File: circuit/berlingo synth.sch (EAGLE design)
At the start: 56 parts, among them IC4 LM358N

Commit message: Changed order and added stereo
Changed order to IN - VCO - VCO~ - LFO - LED - PWM in - PWM~ - PWM out -
FILTER in - FILTER OUT - OUT - OUT

Added L and R
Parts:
- removed C1: 100uF, resistor:C-US050-075X075
- removed JP1: BAT_VIN, adafruit:PINHD-1X1CB
- removed LFO_PHOTO, TRI_PHOTO: PHOTOCELLPTH, SparkFun-Sensors:PHOTOCELLPTH
- removed OUT_C1: 22uF (226), SparkFun-Capacitors:CAPEZ
- removed OUT_R1, OUT_R2: 150, resistor:R-US_0207/10
- added BAT_V+: (no value), wirepad:3,81/1,4
- added C2: 100uF, rcl:CPOL-USE2-4
- added C_OUT_L, C_OUT_R, IN_C2: 226, SparkFun-Capacitors:CAPEZ
- added H6: MOUNT-HOLE2.8, holes:MOUNT-HOLE2.8
- added IN_R: IN(R), TOF:HEADER-1X1
- added IN_R3, IN_R4: 10k, resistor:R-US_0207/10
- added SW1: OS102011MA1Q, adafruit:OS102011MA1Q
- BAT_GND: device adafruit:PINHD-1X1CB -> wirepad:3,81/1,4
- D1: value 1N4004 -> DIODE
- FILTER_IN, FILTER_OUT: value HEADER-1X1 -> FILTER
- FI_C1, FI_C2: value 0.001uF -> 102
- FX_R3: value 1M(or none for full distortion) -> 1M
- H1, H2: value SPECIAL_DRILL_0.1000 -> MOUNT-HOLE2.8; device special-drill:SPECIAL_DRILL_0.1000 -> holes:MOUNT-HOLE2.8
- IN_C1: value 22uF (226) -> 226
- IN_L: value HEADER-1X1 -> IN(L)
- LFO: value HEADER-1X1 -> (none)
- LFO_C3: value 22uF -> 226
- OUTA: value HEADER-1X1 -> OUT(L)
- OUTB: value HEADER-1X1 -> OUT(R)
- PWM_IN, PWM_OUT: value HEADER-1X1 -> PWM
- TRI_C4: value 0.1uF -> 104
- VCO: value HEADER-1X1 -> VCO
- ~LED: value HEADER-1X1 -> ~LED
- ~PWM: value HEADER-1X1 -> ~PWM
- ~VCO: value HEADER-1X1 -> ~VCO
- renumbered FILTER← to FILTER_IN, FILTER→ to FILTER_OUT, IN to IN_L, PWM← to PWM_IN, PWM→ to PWM_OUT, TRI to VCO, ~TRI to ~VCO
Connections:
- new net N$1: BAT_V+.P, SW1G$1.P
- new net N$12: C_OUT_L.1, OUTA.1
- new net N$24: C_OUT_R.2, OUT.RIGHT
- net FILTER_OUT: now also IC4B.OUT; no longer IC4A.OUT
- net GND: now also BAT_GND.P, C2.-, IN_R4.2; no longer BAT_GND.1, C1.2
- net MOD_IN: now also IC4A.+IN; no longer IC4B.+IN
- net N$10: no longer TRI_PHOTO.P$1
- net N$11: now also C_OUT_L.2; no longer OUT.RIGHT, OUT_C1.2
- net N$13: now also C2.+; no longer C1.1
- net N$14: now also IN_C2.1, IN_R.1, IN_R3.2, IN_R4.1; no longer OUTA.1, OUT_R1.1
- net N$15: now also IN_C2.2, JP2.RIGHT; no longer OUT_C1.1, OUT_R1.2, OUT_R2.2
- net N$16: now also IC4B.-IN; no longer IC4A.-IN
- net N$18: no longer TRI_PHOTO.P$2
- net N$21: no longer LFO_PHOTO.P$1
- net N$22: no longer LFO_PHOTO.P$2
- net N$3: now also IC4A.-IN; no longer IC4B.-IN
- net N$7: now also IC4B.+IN; no longer IC4A.+IN
- net N$9: now also C_OUT_R.1; no longer OUT_R2.1
- net PWM_OUT: now also IC4A.OUT; no longer IC4B.OUT
- net VIN: now also IN_R3.1, SW1G$1.O; no longer JP1.1
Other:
- note added: "Remove for full distortion"
- moved on the sheet: IC4A, IC4B, JP2, OUTA

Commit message: Updated Parts and changed a few part names
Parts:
- removed C_OUT_L, C_OUT_R: 226, SparkFun-Capacitors:CAPEZ
- removed D1: DIODE, diode:1N4004
- removed OUTA: OUT(L), TOF:HEADER-1X1
- removed OUTB: OUT(R), TOF:HEADER-1X1
- added OUTL: OUT(L), TOF:HEADER-1X1
- added OUTL_C1, OUTR_C1: 226, SparkFun-Capacitors:CAPEZ
- added OUTR: OUT(R), TOF:HEADER-1X1
- added VCO_DIODE: DIODE, diode:1N4004
- renumbered C2 to LED_C1, FX_R1 to PWM_R1, FX_R2 to PWM_R2, FX_R3 to PWM_R4, FX_R4 to PWM_R3, IC4 to FX_IC, IN_C1 to INL_C1, IN_C2 to INR_C1, IN_L to INL, IN_R to INR, IN_R1 to INL_R1, IN_R2 to INL_R2, IN_R3 to INR_R1, IN_R4 to INR_R2, IN_R8 to VCO_R4, JP2 to IN, LED_LED to LED, LFO_C3 to LFO_C1, TRI_C4 to VCO_C1, TRI_IC to VCO_IC, TRI_PITCH to VCO_PITCH, TRI_R2 to VCO_R3, TRI_R6 to VCO_R1, TRI_R7 to VCO_R2, ~VCO to VCO~
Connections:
- net N$11: now also OUTL_C1.2; no longer C_OUT_L.2
- net N$12: now also OUTL.1, OUTL_C1.1; no longer C_OUT_L.1, OUTA.1
- net N$2: now also VCO_DIODE.C; no longer D1.C
- net N$24: now also OUTR_C1.2; no longer C_OUT_R.2
- net N$9: now also OUTR.1, OUTR_C1.1; no longer C_OUT_R.1, OUTB.1
- net TRIANGLE_PITCHMOD: now also VCO_DIODE.A; no longer D1.A
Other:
- note added: "Use eagle 6.6 to export"

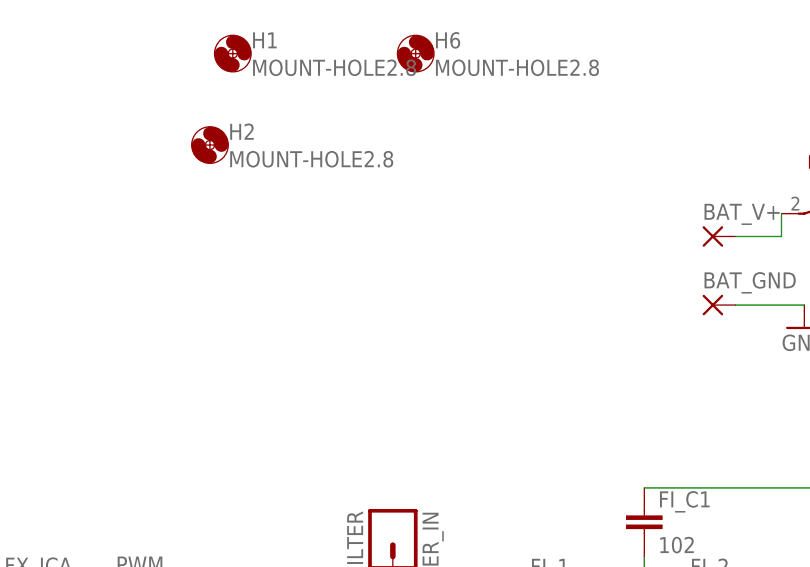
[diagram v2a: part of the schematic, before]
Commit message: Update BOM, increased trace sizes and added more silkscreen info
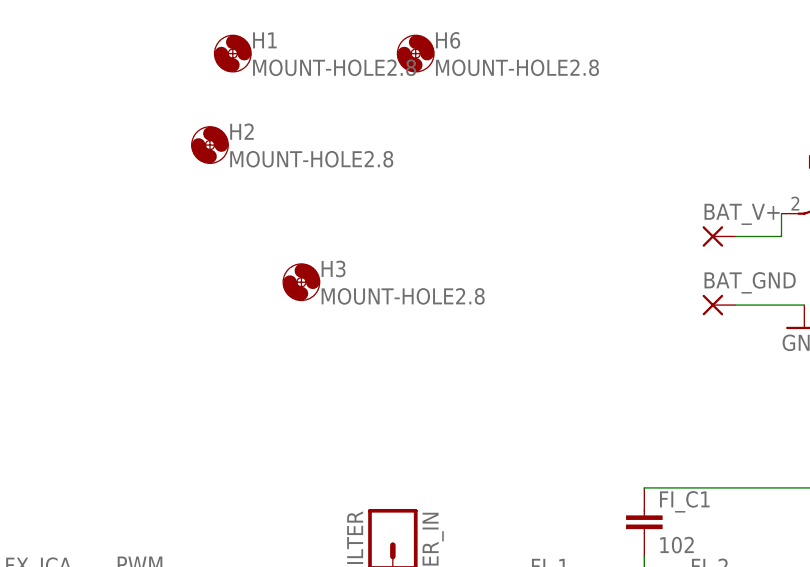
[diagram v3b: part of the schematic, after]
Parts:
- added H3: MOUNT-HOLE2.8, holes:MOUNT-HOLE2.8
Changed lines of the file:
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@@
 <grid distance="0.1" unitdist="inch" unit="inch" style="lines" multiple="1" display="no" altdistance="0.01" altunitdist="inch" altunit="inch"/>
 <layers>
-<layer number="1" name="Top" color="4" fill="1" visible="no" active="no"/>
-<layer number="16" name="Bottom" color="1" fill="1" visible="no" active="no"/>
-<layer number="17" name="Pads" color="2" fill="1" visible="no" active="no"/>
-<layer number="18" name="Vias" color="2" fill="1" visible="no" active="no"/>
-<layer number="19" name="Unrouted" color="6" fill="1" visible="no" active="no"/>
-<layer number="20" name="Dimension" color="15" fill="1" visible="no" active="no"/>
-<layer number="21" name="tPlace" color="7" fill="1" visible="no" active="no"/>
-<layer number="22" name="bPlace" color="7" fill="1" visible="no" active="no"/>
-<layer number="23" name="tOrigins" color="15" fill="1" visible="no" active="no"/>
-<layer number="24" name="bOrigins" color="15" fill="1" visible="no" active="no"/>
-<layer number="25" name="tNames" color="7" fill="1" visible="no" active="no"/>
-<layer number="26" name="bNames" color="7" fill="1" visible="no" active="no"/>
-<layer number="27" name="tValues" color="7" fill="1" visible="no" active="no"/>
-<layer number="28" name="bValues" color="7" fill="1" visible="no" active="no"/>
+<layer number="1" name="Top" color="4" fill="1" visible="yes" active="no"/>
+<layer number="16" name="Bottom" color="1" fill="1" visible="yes" active="no"/>
+<layer number="17" name="Pads" color="2" fill="1" visible="yes" active="no"/>
+<layer number="18" name="Vias" color="2" fill="1" visible="yes" active="no"/>
+<layer number="19" name="Unrouted" color="6" fill="1" visible="yes" active="no"/>
+<layer number="20" name="Dimension" color="15" fill="1" visible="yes" active="no"/>
+<layer number="21" name="tPlace" color="7" fill="1" visible="yes" active="no"/>
+<layer number="22" name="bPlace" color="7" fill="1" visible="yes" active="no"/>
+<layer number="23" name="tOrigins" color="15" fill="1" visible="yes" active="no"/>
+<layer number="24" name="bOrigins" color="15" fill="1" visible="yes" active="no"/>
+<layer number="25" name="tNames" color="7" fill="1" visible="yes" active="no"/>
+<layer number="26" name="bNames" color="7" fill="1" visible="yes" active="no"/>
+<layer number="27" name="tValues" color="7" fill="1" visible="yes" active="no"/>
+<layer number="28" name="bValues" color="7" fill="1" visible="yes" active="no"/>
 <layer number="29" name="tStop" color="7" fill="3" visible="no" active="no"/>
 <layer number="30" name="bStop" color="7" fill="6" visible="no" active="no"/>
@@
 <layer number="35" name="tGlue" color="7" fill="4" visible="no" active="no"/>
 <layer number="36" name="bGlue" color="7" fill="5" visible="no" active="no"/>
-<layer number="37" name="tTest" color="7" fill="1" visible="no" active="no"/>
-<layer number="38" name="bTest" color="7" fill="1" visible="no" active="no"/>
+<layer number="37" name="tTest" color="7" fill="1" visible="yes" active="no"/>
+<layer number="38" name="bTest" color="7" fill="1" visible="yes" active="no"/>
 <layer number="39" name="tKeepout" color="4" fill="11" visible="no" active="no"/>
 <layer number="40" name="bKeepout" color="1" fill="11" visible="no" active="no"/>
@@
 <layer number="44" name="Drills" color="7" fill="1" visible="no" active="no"/>
 <layer number="45" name="Holes" color="7" fill="1" visible="no" active="no"/>
-<layer number="46" name="Milling" color="3" fill="1" visible="no" active="no"/>
-<layer number="47" name="Measures" color="7" fill="1" visible="no" active="no"/>
-<layer number="48" name="Document" color="7" fill="1" visible="no" active="no"/>
-<layer number="49" name="Reference" color="7" fill="1" visible="no" active="no"/>
-<layer number="50" name="dxf" color="7" fill="1" visible="no" active="no"/>
-<layer number="51" name="tDocu" color="7" fill="1" visible="no" active="no"/>
-<layer number="52" name="bDocu" color="7" fill="1" visible="no" active="no"/>
-<layer number="53" name="tGND_GNDA" color="7" fill="9" visible="no" active="no"/>
-<layer number="54" name="bGND_GNDA" color="1" fill="9" visible="no" active="no"/>
-<layer number="56" name="wert" color="7" fill="1" visible="no" active="no"/>
-<layer number="57" name="tCAD" color="7" fill="1" visible="no" active="no"/>
-<layer number="59" name="tCarbon" color="7" fill="1" visible="no" active="no"/>
-<layer number="60" name="bCarbon" color="7" fill="1" visible="no" active="no"/>
+<layer number="46" name="Milling" color="3" fill="1" visible="yes" active="no"/>
+<layer number="47" name="Measures" color="7" fill="1" visible="yes" active="no"/>
+<layer number="48" name="Document" color="7" fill="1" visible="yes" active="no"/>
+<layer number="49" name="Reference" color="7" fill="1" visible="yes" active="no"/>
+<layer number="50" name="dxf" color="7" fill="1" visible="yes" active="no"/>
+<layer number="51" name="tDocu" color="7" fill="1" visible="yes" active="no"/>
+<layer number="52" name="bDocu" color="7" fill="1" visible="yes" active="no"/>
+<layer number="53" name="tGND_GNDA" color="7" fill="9" visible="yes" active="no"/>
+<layer number="54" name="bGND_GNDA" color="1" fill="9" visible="yes" active="no"/>
+<layer number="56" name="wert" color="7" fill="1" visible="yes" active="no"/>
+<layer number="57" name="tCAD" color="7" fill="1" visible="yes" active="no"/>
+<layer number="59" name="tCarbon" color="7" fill="1" visible="yes" active="no"/>
+<layer number="60" name="bCarbon" color="7" fill="1" visible="yes" active="no"/>
 <layer number="90" name="Modules" color="5" fill="1" visible="yes" active="yes"/>
 <layer number="91" name="Nets" color="2" fill="1" visible="yes" active="yes"/>
@@
 <part name="SUPPLY3" library="SparkFun-Aesthetics" deviceset="VIN" device=""/>
 <part name="GND8" library="SparkFun-Aesthetics" deviceset="GND" device=""/>
+<part name="H3" library="holes" deviceset="MOUNT-HOLE" device="2.8"/>
 </parts>
 <sheets>
@@
 <instance part="SUPPLY3" gate="G$1" x="160.02" y="86.36"/>
 <instance part="GND8" gate="1" x="160.02" y="55.88"/>
+<instance part="H3" gate="G$1" x="35.56" y="40.64"/>
 </instances>
 <busses>

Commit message: Euh...
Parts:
- added LED_C2: 100uF, rcl:CPOL-USE2.5-6
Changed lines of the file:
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@@
 <part name="GND8" library="SparkFun-Aesthetics" deviceset="GND" device=""/>
 <part name="H3" library="holes" deviceset="MOUNT-HOLE" device="2.8"/>
+<part name="LED_C2" library="rcl" deviceset="CPOL-US" device="E2.5-6" value="100uF"/>
 </parts>
 <sheets>
@@
 <instance part="GND8" gate="1" x="160.02" y="55.88"/>
 <instance part="H3" gate="G$1" x="35.56" y="40.64"/>
+<instance part="LED_C2" gate="G$1" x="233.68" y="55.88"/>
 </instances>
 <busses>
